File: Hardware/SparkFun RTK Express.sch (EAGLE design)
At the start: 123 parts, among them J13 Internal, J16 microSD, J17 Qwiic Right Angle, J19 FPC_12_0.5MM_BACKFLIP, J3 USB Female Type C Connector, J4 External, J5 USB Female Type C Connector, Q1 SIL2308-TP, Q10 20V/0.2A/8MHz/1.2Ω/1Vth, Q2 MBT3904DW1T1, Q3 20V/0.2A/8MHz/1.2Ω/1Vth, Q4 20V/0.2A/8MHz/1.2Ω/1Vth, Q7 20V/0.2A/8MHz/1.2Ω/1Vth, Q9 20V/0.2A/8MHz/1.2Ω/1Vth, U1 74HC4052D, U10 MCP73833, U13 9DoF IMU, U14 1.8V/100mA, U2 AP2112K-3.3, U3 U-BLOX_ZED-F9P, U4 ADP160, U5 ESP-WROOM-32NARROW, U6 CH340C, U7 MAX17048

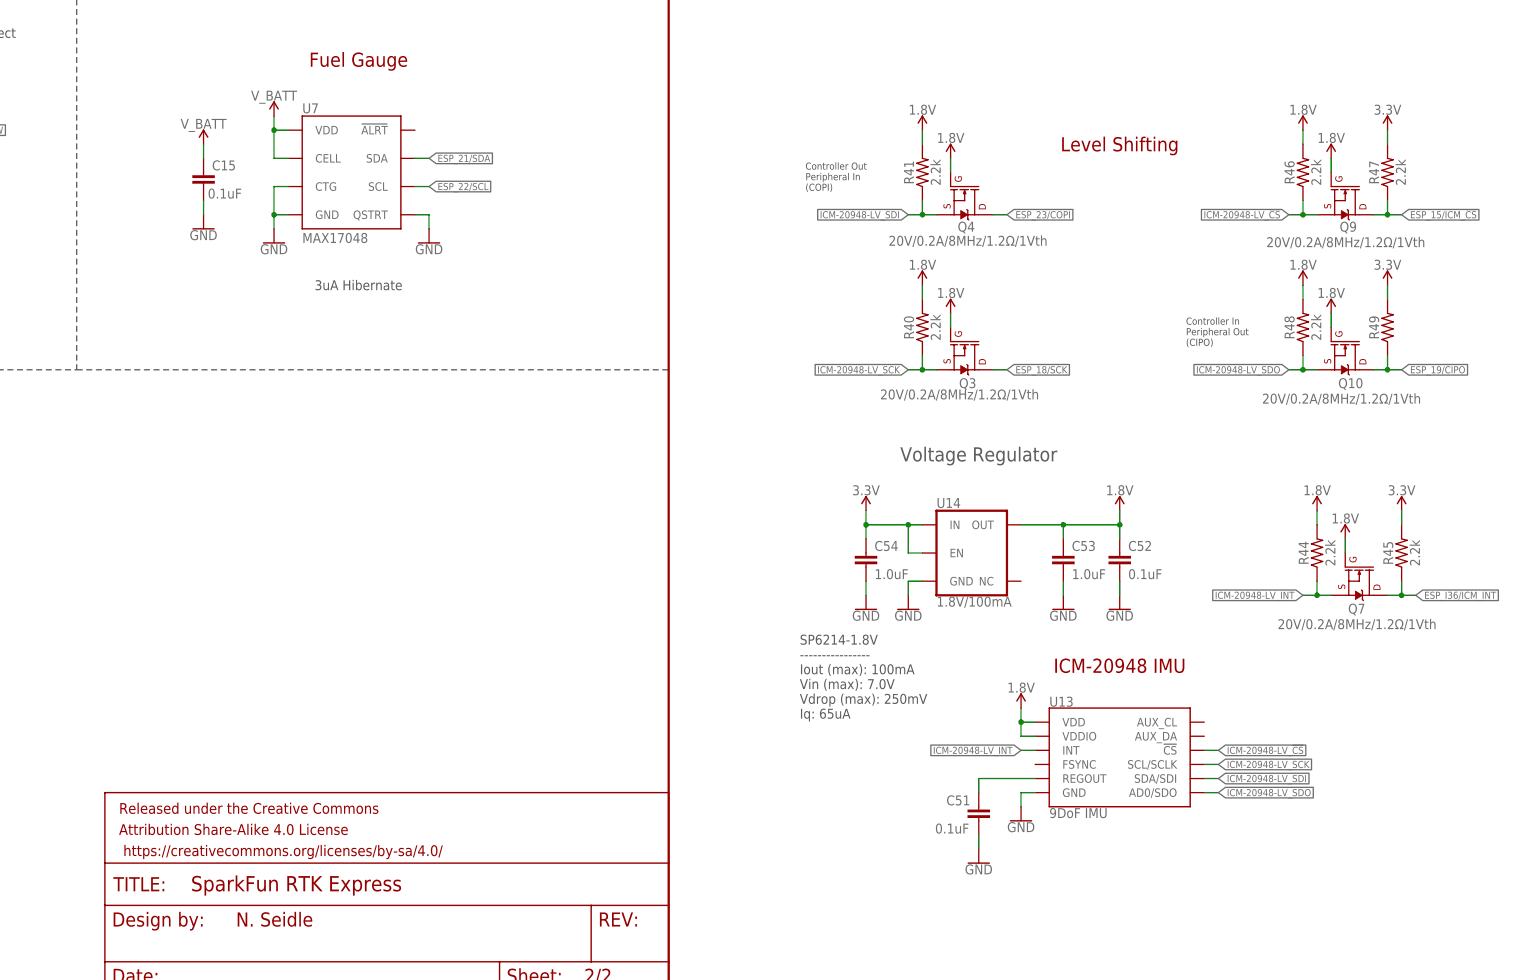
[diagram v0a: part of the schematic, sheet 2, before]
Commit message: Ready v11. Redo GND layers for panelizer.
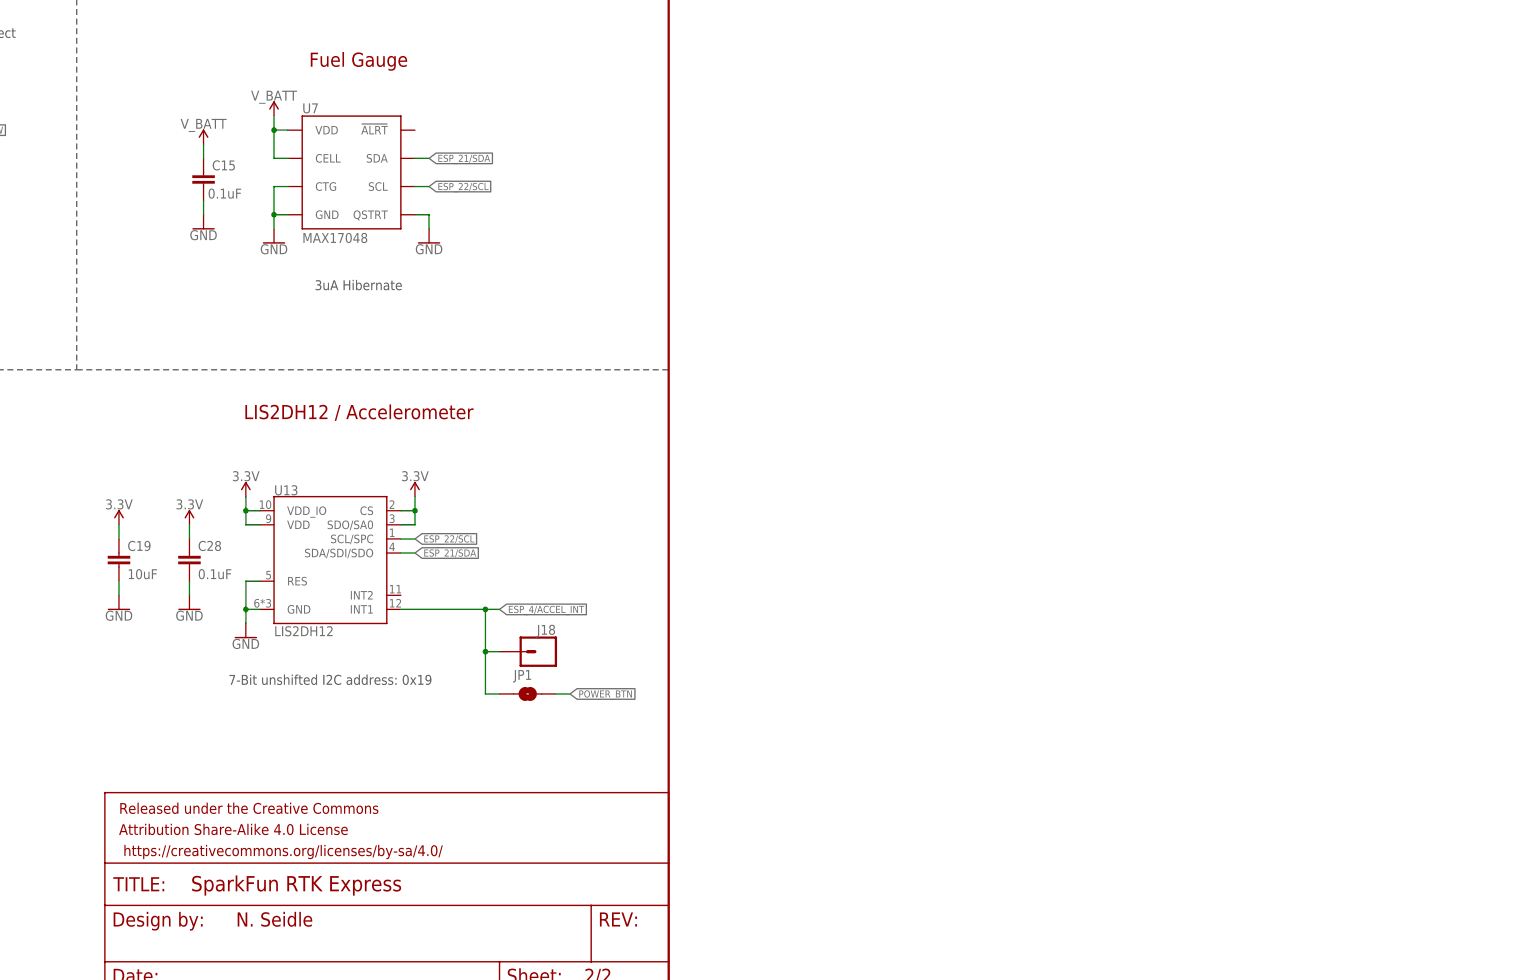
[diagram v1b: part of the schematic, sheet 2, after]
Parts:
- removed C51: 0.1uF, SparkFun-Capacitors:0.1UF-0603-100V-10%
- removed C52: 0.1uF, SparkFun-Capacitors:0.1UF-0603-25V-(+80/-20%)
- removed C53, C54: 1.0uF, SparkFun-Capacitors:1.0UF-0603-16V-10%
- removed D4: BLUE, SparkFun-LED:LED-BLUE0603
- removed D5: RGB, SparkFun-LED:LED-RGBPLCC-6
- removed Q10, Q3, Q4, Q7, Q9: 20V/0.2A/8MHz/1.2Ω/1Vth, SparkFun-DiscreteSemi:MOSFET-NCH-RE1C00UNTL
- removed R10: 330, SparkFun-Resistors:330OHM-0603-1/10W-1%
- removed R40, R41, R44, R45, R46, R47, R48: 2.2k, SparkFun-Resistors:2.2KOHM-0603-1/10W-1%
- removed R49: (no value), SparkFun-Resistors:RESISTOR0603
- removed R6, R8: 1k, SparkFun-Resistors:1KOHM-0603-1/10W-1%
- removed S2: Setup, SparkFun-Switches:MOMENTARY-SWITCH-SPST-PTH-6.0MM
- removed S3: Power, SparkFun-Switches:MOMENTARY-SWITCH-SPST-SMD-12MM
- removed S4: Setup, SparkFun-Switches:MOMENTARY-SWITCH-SPST-SMD-12MM
- removed U14: 1.8V/100mA, SparkFun-IC-Power:V_REG_SP6214-1.8V
- added C19: 10uF, SparkFun-Capacitors:10UF-0603-6.3V-20%
- added C21, C28: 0.1uF, SparkFun-Capacitors:0.1UF-0603-25V-(+80/-20%)
- added J18: (no value), SparkFun-Connectors:CONN_01PTH_NO_SILK_YES_STOP
- added JP1: JUMPER-SMT_2_NO_SILK, SparkFun-Jumpers:JUMPER-SMT_2_NO_SILK
- BT1: value LIPO-OUTLINE1100 -> LIPO-OUTLINE1000; device SparkFun-Batteries:LIPO-OUTLINE1100 -> SparkFun-Batteries:LIPO-OUTLINE1000
- R1: value 4.7k -> 470; device SparkFun-Resistors:4.7KOHM-0603-1/10W-1% -> SparkFun-Resistors:470OHM-0603-1/10W-1%
- S1: device SparkFun-Switches:MOMENTARY-SWITCH-SPST-PTH-6.0MM -> SparkFun-Switches:MOMENTARY-SWITCH-SPST-SMD-5.2MM-TALL
- U13: value 9DoF IMU -> LIS2DH12; device SparkFun-Sensors:ICM-20948 -> SparkFun-Sensors:LIS2DH12
- U5: value ESP-WROOM-32NARROW -> ESP-WROOM-3232D-NARROW; device SparkFun-RF:ESP-WROOM-32NARROW -> SparkFun-RF:ESP-WROOM-3232D-NARROW
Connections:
- net RTC_BACKUP renamed V_BKCP
- removed net ESP_12/LED_BLUETOOTH: R10.1, U5.MISO_H/IO12
- removed net ESP_15/ICM_!CS!: Q9.D, R47.1, U5.CS0_H/IO15
- removed net ESP_32/PWR_LVL_RED: D5.RED-A, U5.XTAL_P/IO32
- removed net ESP_33/PWR_LVL_GRN: D5.GRN-A, U5.XTAL_N/IO33
- removed net ESP_I36/ICM_INT: Q7.D, R45.1, U5.SENSOR_VP/I36
- removed net ICM-20948-LV_!CS!: Q9.S, R46.1, U13.!CS
- removed net ICM-20948-LV_#_1.8V: C52.1, C53.1, Q10.G, Q3.G, Q4.G, Q7.G, Q9.G, R40.2, R41.2, R44.2, R46.2, R48.2, U13.VDD, U13.VDDIO, U14.OUT
- removed net ICM-20948-LV_INT: Q7.S, R44.1, U13.INT
- removed net ICM-20948-LV_SCK: Q3.S, R40.1, U13.SCL/SCLK
- removed net ICM-20948-LV_SDI: Q4.S, R41.1, U13.SDA/SDI
- removed net ICM-20948-LV_SDO: Q10.S, R48.1, U13.AD0/SDO
- removed net N$10: D5.GRN-C, R6.1
- removed net N$14: D5.RED-C, R8.1
- removed net N$3: D4.A, R10.2
- removed net N$30: C51.1, U13.REGOUT
- new net ESP_12: U5.MISO2/IOA12
- new net ESP_15: U5.CS2/IOA15
- new net ESP_32: U5.XTAL_P/IOA32
- new net ESP_33: U5.XTAL_N/IOA33
- new net ESP_4/ACCEL_INT: J18.1, JP1.1, U13.INT1
- new net ESP_I36: U5.SENSOR_VP/IA36
- net 3.3V: now also C19.1, C28.1, U13.CS, U13.SDO/SA0, U13.VDD, U13.VDD_IO; no longer C54.1, R45.2, R47.2, R49.2, U14.EN, U14.IN
- net CHG_LED: no longer J19.10, J19.9
- net CHG_LED_RES: now also J19.10, J19.9; no longer D5.BLU-C
- net ESP32_RXI: now also U5.RX-IO3; no longer U5.RXD
- net ESP32_TXO: now also U5.TX-IO1; no longer U5.TXD
- net ESP_0/BOOT: now also U5.IOA0; no longer U5.IO0
- net ESP_13/POWER_CTRL: now also U5.MOSI2/IOA13; no longer U5.MOSI_H/IO13
- net ESP_14/SETUP_BUTTON: now also C21.1, U5.SCK2/IOA14; no longer S2.1, S4.1, U5.SCK_H/IO14
- net ESP_18/SCK: now also U5.SCK3/IO18; no longer Q3.D, U5.SCK_V/IO18
- net ESP_19/CIPO: now also U5.MISO3/IO19; no longer Q10.D, R49.1, U5.MISO_V/IO19
- net ESP_2/MUX_A: now also U5.IOA2; no longer U5.IO2
- net ESP_21/SDA: now also U13.SDA/SDI/SDO, U5.SDA/IO21; no longer U5.IO21
- net ESP_22/SCL: now also U13.SCL/SPC, U5.SCL/IO22; no longer U5.IO22
- net ESP_23/COPI: now also U5.MOSI3/IO23; no longer Q4.D, U5.MOSI_V/IO23
- net ESP_25/SD_!CS!: now also U5.DAC1/IOA25; no longer U5.IO25
- net ESP_26/DAC2: now also U5.DAC2/IOA26; no longer U5.IO26
- net ESP_27/FAST_OFF: now also U5.IOA27; no longer U5.IO27
- net ESP_4/MUX_B: now also U5.IOA4; no longer U5.IO4
- net ESP_5: now also U5.CS3/IO5; no longer U5.CS0_V/IO5
- net ESP_I34/ZED_TX_READY: now also U5.IA34; no longer U5.I34
- net ESP_I35: now also U5.IA35; no longer U5.I35
- net ESP_I39/ADC39: now also U5.SENSOR_VN/IA39; no longer U5.SENSOR_VN/I39
- net GND: now also C19.2, C21.2, C28.2, U13.RES; no longer C51.2, C52.2, C53.2, C54.2, D4.C, R6.2, R8.2, S2.2, S3.2, S4.2, U14.GND
- net POWER_BTN: now also JP1.2; no longer S3.1
- net V_USB: no longer D5.BLU-A
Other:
- note added: "(Done) Add fast off"
- note added: "(Done) Change to LIS Accel"
- note added: "(Done) Remove LEDs"
- note added: "(Done) add 12 pin membrane connector"
- note added: "(Done) add debounce cap to setup button"
- note added: "7-Bit unshifted I2C address: 0x19"
- note added: "ADC2 has problems when WiFi is enabled."
- note added: "IO0: Avoid device connections. Can be used as a stat LED."
- note added: "IO12: Avoid external pullups - will cause bootloader fail."
- note added: "IO15: Has builtin pullup at POR."
- note added: "IO2: Avoid external pullups - will cause bootloader fail."
- note added: "IO5: Has builtin pullup at POR."
- note added: "LIS2DH12 / Accelerometer"
- note added: "Use boot control pins with caution: 0, 2, 5, 12, 15"
- note removed: "Add fast off"
- note removed: "Bluetooth Status"
- note removed: "Change power off cap to 22uF"
- note removed: "Change to LIS Accel"
- note removed: "Controller In Peripheral Out (CIPO)"
- note removed: "Controller Out Peripheral In (COPI)"
- note removed: "ICM-20948 IMU"
- note removed: "Level Shifting"
- note removed: "Remove LEDs"
- note removed: "SP6214-1.8V ---------------- Iout (max): 100mA Vin (max): 7.0V Vdrop (max): 250mV Iq: 65uA"
- note removed: "Stat LEDs"
- note removed: "Voltage Regulator"
- note removed: "add 12 pin membrane connector"
- note removed: "add debounce cap to setup button"
- moved on the sheet: R1, R19

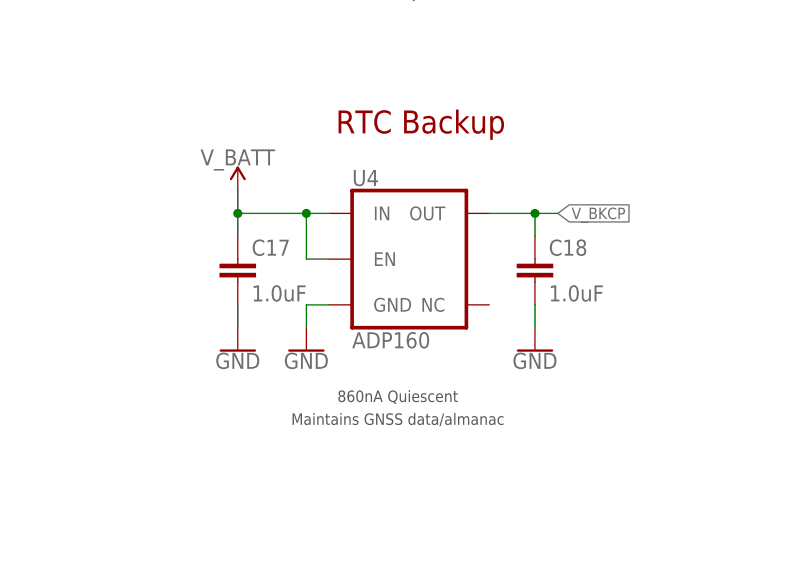
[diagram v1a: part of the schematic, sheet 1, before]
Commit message: Update FP and PROD ID on ESP32 module
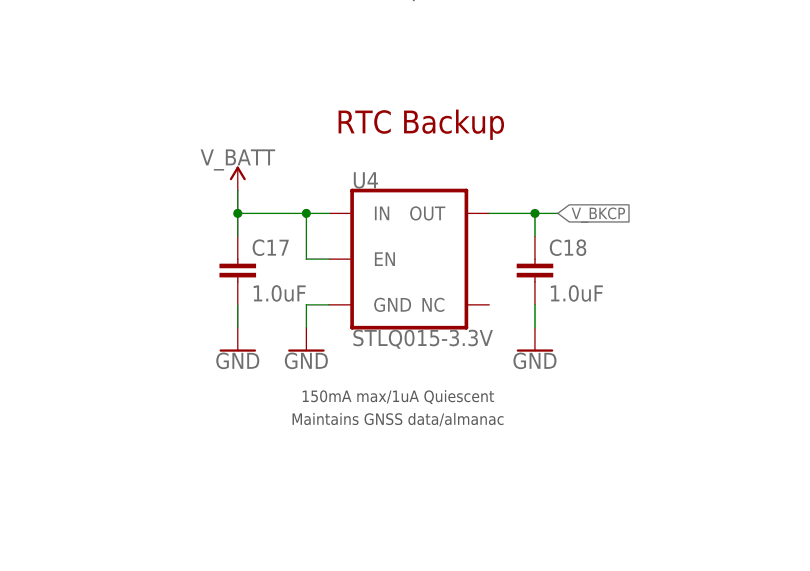
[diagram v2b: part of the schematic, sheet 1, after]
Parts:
- U4: value ADP160 -> STLQ015-3.3V; device SparkFun-IC-Power:ADP160 -> SparkFun-IC-Power:STLQ015-3.3V
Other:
- note added: "150mA max/1uA Quiescent"
- note removed: "860nA Quiescent"

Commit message: Move radio to power control. Add ESD to GNSS RF. Move overlay connector.
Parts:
- removed J19: FPC_12_0.5MM_BACKFLIP, RTK Facet:FPC_12_0.5MM_BACKFLIP
- added D10: PESD0402, New_Parts:PESD0402
- added J20: FPC_12_0.5MM_BACKFLIP, RTK Facet:FPC_12_0.5MM_BACKFLIP
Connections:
- net CHG_LED_RES: now also J20.3, J20.4; no longer J19.10, J19.9
- net ESP_14/SETUP_BUTTON: now also J20.7, J20.8; no longer J19.5, J19.6
- net GND: now also D10.2, J20.11, J20.12; no longer J19.1, J19.2
- net GPS_ANT1: now also D10.1
- net POWER_BTN: now also J20.10, J20.9; no longer J19.3, J19.4
- net VOUT: now also J11.4, J9.1
- net V_RAW: no longer J11.4, J9.1
- net V_USB: now also J20.1, J20.2; no longer J19.11, J19.12
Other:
- note added: "v12"
- note removed: "(Done) Add fast off"
- note removed: "(Done) Change to LIS Accel"
- note removed: "(Done) Remove LEDs"
- note removed: "(Done) add 12 pin membrane connector"
- note removed: "(Done) add debounce cap to setup button"
- note removed: "breakout swd?"
- note removed: "v13"
- moved on the sheet: C1, C2, C7, E1, FB1, R14, R15, R27, R28, R2A, R2B, R2C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

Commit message: Add PROD_ID for PESD diode.
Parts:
- D10: device New_Parts:PESD0402 -> SparkFun-DiscreteSemi:PESD0402
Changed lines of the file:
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@@
 <part name="SUPPLY18" library="SparkFun-PowerSymbols" deviceset="VOUT" device=""/>
 <part name="SUPPLY23" library="SparkFun-PowerSymbols" deviceset="VOUT" device=""/>
-<part name="D10" library="New_Parts" deviceset="PESD0402" device=""/>
+<part name="D10" library="SparkFun-DiscreteSemi" deviceset="PESD0402" device=""/>
 <part name="GND9" library="SparkFun-PowerSymbols" deviceset="GND" device=""/>
 <part name="J20" library="RTK Facet" deviceset="FPC_12_0.5MM" device="_BACKFLIP" value="FPC_12_0.5MM_BACKFLIP"/>

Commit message: Shuffle schematic elements to fit into frame.
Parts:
- removed FRAME1: FRAME-LETTERNO_PACKAGE, SparkFun-Aesthetics:FRAME-LETTERNO_PACKAGE
- added FRAME3: FRAME-LEDGERNO_FOOTPRINT, SparkFun-Aesthetics:FRAME-LEDGERNO_FOOTPRINT
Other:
- note added: "Soft Power Switch"
- moved on the sheet: C1, C15, C19, C2, C20, C22, C23, C28, C7, C8, C9, D1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
